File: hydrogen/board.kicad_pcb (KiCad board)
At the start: 2 copper layers, 70.1 x 22.5 mm, 40 parts, among them J1 Power, J10 OUT B3, J11 OUT B4, J2 IN A, J3 OUT A1, J4 OUT A2, J5 OUT A3, J6 OUT A4, J7 IN B, J8 OUT B1, J9 OUT B2, U1 OPA4991, U2 OPA4991, U3 LM358

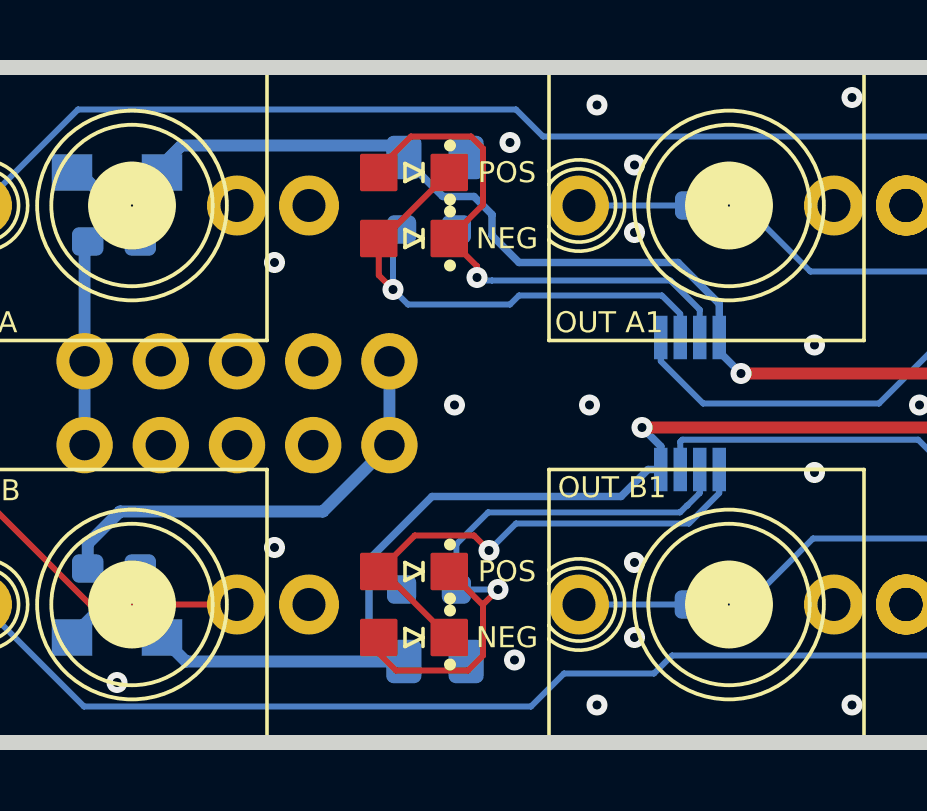
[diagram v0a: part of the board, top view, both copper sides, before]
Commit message: Rename folders
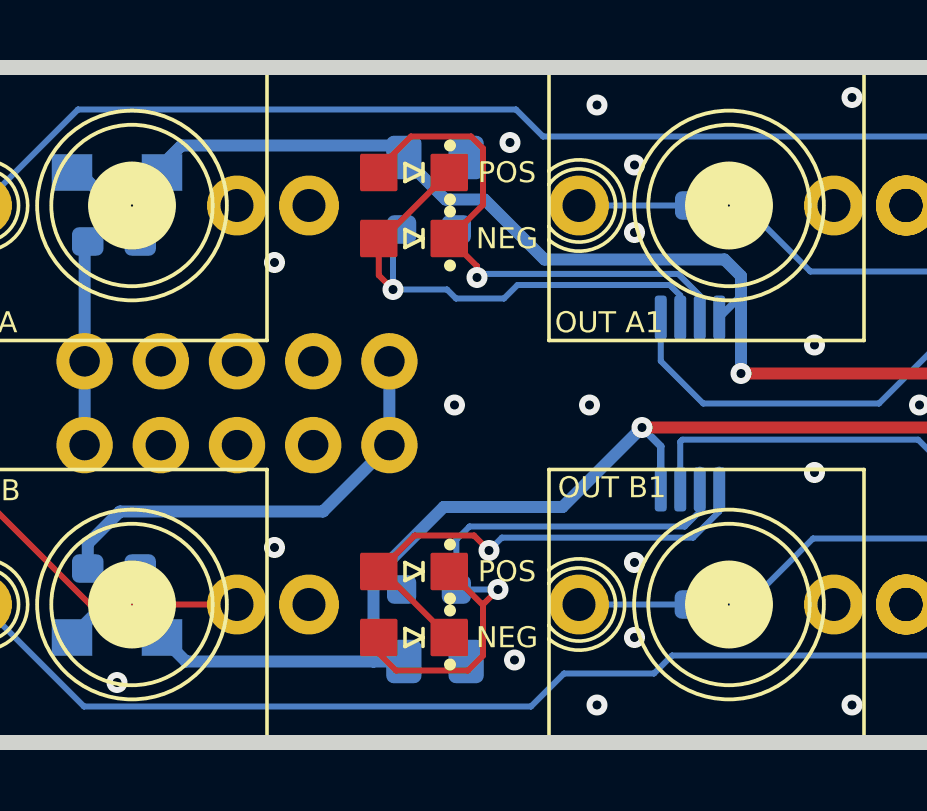
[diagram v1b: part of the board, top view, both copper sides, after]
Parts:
- U3: footprint Package_SO:VSSOP-8_3.0x3.0mm_P0.65mm -> Package_SO:TSSOP-8_4.4x3mm_P0.65mm
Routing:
- net +12V: track 70.2 -> 72.1 mm
- net -12V: track 78.3 -> 77.3 mm
- net Net-(D5-Pad1): track 20.9 -> 21.5 mm
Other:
- board text added: "Hydrogen v2 10/7/2021"
- board text removed: "Hydrogen v2 10/2/2021"
